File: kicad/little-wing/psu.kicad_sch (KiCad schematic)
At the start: 14 parts, among them J1 HRO_TYPE-C-31-M-14, J2 Battery, SW1 Battery, U2 ${ALTIUM_VALUE}

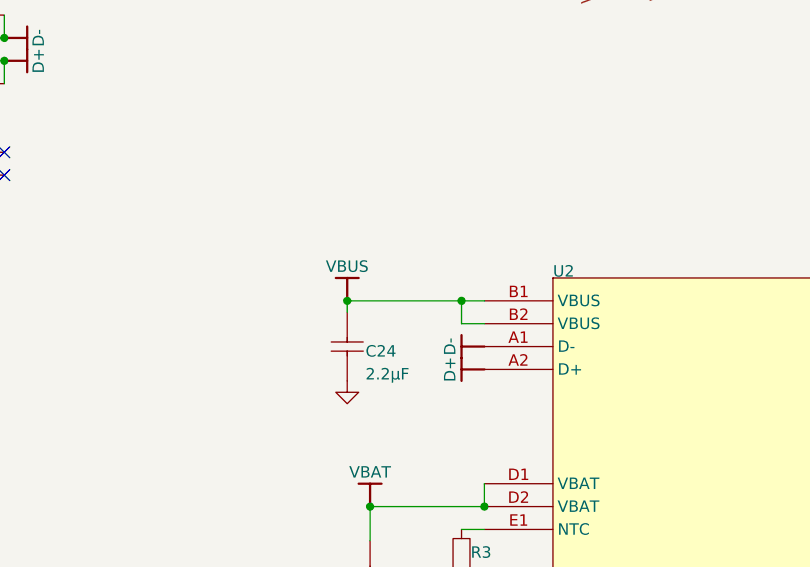
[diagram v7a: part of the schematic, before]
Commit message: Backporting footprints from the PCB back to schematic
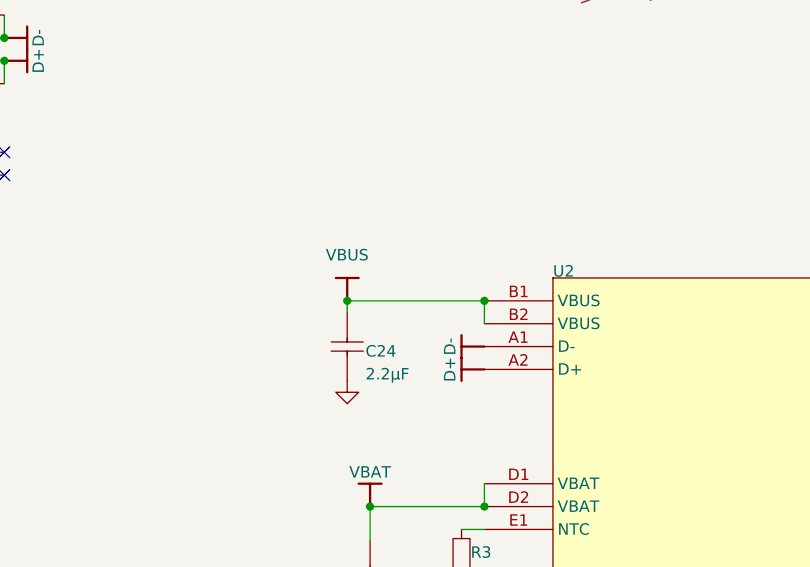
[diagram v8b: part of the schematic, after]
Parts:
- C22: footprint CAPC0603X03L_C -> Capacitor_SMD:C_0201_0603Metric
- C23, C24: footprint CAPC1608X06L -> Capacitors$:CAPC1608X06L
- SW1: footprint (none) -> ScottoKeebs_Components:Switch_MSK12C02
- U2: footprint BGA25C40P5X5_200X200X50 -> nRF Devices$:BGA25C40P5X5_200X200X50
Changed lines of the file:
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@@
 	)
 	(junction
+		(at 88.9 72.39)
+		(diameter 0)
+		(color 0 0 0 0)
+	)
+	(junction
 		(at 165.1 74.93)
 		(diameter 0)
@@
 	)
 	(junction
-		(at 101.6 72.39)
-		(diameter 0)
-		(color 0 0 0 0)
-	)
-	(junction
 		(at 91.44 95.25)
 		(diameter 0)
@@
 	)
 	(junction
-		(at 88.9 72.39)
+		(at 104.14 72.39)
 		(diameter 0)
 		(color 0 0 0 0)
@@
 	(wire
 		(pts
-			(xy 88.9 72.39) (xy 88.9 73.66)
+			(xy 59.69 27.94) (xy 50.8 27.94)
 		)
 		(stroke
@@
 	(wire
 		(pts
-			(xy 59.69 27.94) (xy 50.8 27.94)
+			(xy 50.8 45.72) (xy 50.8 48.26)
 		)
 		(stroke
@@
 	(wire
 		(pts
-			(xy 50.8 45.72) (xy 50.8 48.26)
+			(xy 101.6 106.68) (xy 101.6 105.41)
 		)
 		(stroke
@@
 	(wire
 		(pts
-			(xy 101.6 106.68) (xy 101.6 105.41)
+			(xy 88.9 72.39) (xy 88.9 73.66)
 		)
 		(stroke
@@
 	(wire
 		(pts
-			(xy 101.6 72.39) (xy 104.14 72.39)
-		)
-		(stroke
-			(width 0)
-			(type default)
-		)
-	)
-	(wire
-		(pts
 			(xy 91.44 95.25) (xy 104.14 95.25)
 		)
@@
 	(wire
 		(pts
-			(xy 104.14 74.93) (xy 101.6 74.93)
-		)
-		(stroke
-			(width 0)
-			(type default)
-		)
-	)
-	(wire
-		(pts
 			(xy 205.74 99.06) (xy 205.74 74.93)
 		)
@@
 	(wire
 		(pts
-			(xy 101.6 72.39) (xy 88.9 72.39)
+			(xy 86.36 125.73) (xy 91.44 125.73)
 		)
 		(stroke
@@
 	(wire
 		(pts
-			(xy 86.36 125.73) (xy 91.44 125.73)
+			(xy 104.14 72.39) (xy 104.14 74.93)
 		)
 		(stroke
@@
 	(wire
 		(pts
-			(xy 101.6 74.93) (xy 101.6 72.39)
+			(xy 88.9 72.39) (xy 104.14 72.39)
 		)
 		(stroke
@@
 			)
 		)
-		(property "Footprint" ""
+		(property "Footprint" "ScottoKeebs_Components:Switch_MSK12C02"
 			(at 46.99 106.68 0)
 			(effects
@@
 			)
 		)
-		(property "Footprint" "BGA25C40P5X5_200X200X50"
+		(property "Footprint" "nRF Devices$:BGA25C40P5X5_200X200X50"
 			(at 111.76 69.85 0)
 			(effects
@@
 		(on_board yes)
 		(dnp no)
+		(fields_autoplaced yes)
 		(property "Reference" "#PWR044"
 			(at 88.9 72.39 0)
@@
 		)
 		(property "Value" "VBUS"
-			(at 88.9 68.58 0)
+			(at 88.9 67.31 0)
 			(effects
 				(font
@@
 			)
 		)
-		(property "Footprint" "CAPC1608X06L"
+		(property "Footprint" "Capacitors$:CAPC1608X06L"
 			(at 88.9 81.28 0)
 			(effects
@@
 			)
 		)
-		(property "Footprint" "CAPC1608X06L"
+		(property "Footprint" "Capacitors$:CAPC1608X06L"
 			(at 182.88 85.09 0)
 			(effects
@@
 			)
 		)
-		(property "Footprint" "CAPC0603X03L_C"
+		(property "Footprint" "Capacitor_SMD:C_0201_0603Metric"
 			(at 91.44 106.68 0)
 			(effects
